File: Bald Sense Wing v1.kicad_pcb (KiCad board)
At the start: 4 copper layers, 50.8 x 22.9 mm, 43 parts, among them J1 feather long, J2 feather short, J3 1140084168, Q1 Q_PNP_BEC, Q2 Q_NPN_BEC, U1 APDS-9960, U2 DS3231MZ, U3 SHT30-DIS, U4 MIC5504-3.3YM5, U5 CMM-4737DT-26186-TR

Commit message: Finished v1 layout
Thanks to everyone on the stream!
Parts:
- moved JP6 18.3 mm to (61.6, 38.5)
- moved JP2 2.49 mm to (50.6, 35.6), turned to 90 degrees
- moved JP1 1.88 mm to (34.0, 43.9), turned to 0 degrees
- moved C1 1.80 mm to (69.9, 42.4)
- moved C4 0.84 mm to (69.1, 36.7), turned to 270 degrees
- moved U3 0.13 mm to (73.5, 36.7), turned to 180 degrees
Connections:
- J1 pad 11: /SD-CS -> /SD_CS
- J1 pad 12: /SD-CD -> /SD_CD
- J1 pad 8: /SHT30-ALERT -> /Batt_Meas
- J1 pad 9: /Batt_Meas -> /Batt_Meas_En
- J2 pad 3: /PDM_CLK -> /DS3231_RST
- J2 pad 4: /PDM_DATA -> /DS3231_INT
- J2 pad 5: /DS3231_RST -> /32KHz
- J2 pad 6: /DS3231_INT -> /PDM_CLK
- J2 pad 7: /32KHz -> /PDM_DATA
- J2 pad 8: /Batt_Meas_En -> /SHT30_ALERT
- JP3 pad 2: /SHT30-ALERT -> /SHT30_ALERT
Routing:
- net +BATT: track 0.00 -> 56.5 mm, vias 0 -> 2
- net +3V3: track 0.00 -> 45.4 mm, vias 0 -> 8
- net /VBAT: track 0.00 -> 38.1 mm, vias 0 -> 1
- net GND: track 0.00 -> 34.7 mm, vias 0 -> 19
- net /APDS_INT: track 0.00 -> 32.9 mm, vias 0 -> 4
- net /PDM_DATA: track 0.00 -> 32.7 mm
- net /PDM_CLK: track 0.00 -> 30.9 mm
- net /SD_DIn: track 0.00 -> 29.5 mm, vias 0 -> 1
- net /SD_CD: track 0.00 -> 28.5 mm
- net /VUSB_Meas: track 0.00 -> 28.4 mm
- net /SCL: track 2.77 -> 29.9 mm, vias 0 -> 2
- net /SD_DOut: track 0.00 -> 27.0 mm, vias 0 -> 2
- net /SD_CLK: track 0.00 -> 25.6 mm, vias 0 -> 1
- net /SDA: track 2.77 -> 27.9 mm, vias 0 -> 1
- net /SHT30_ALERT: track 0.00 -> 24.8 mm
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- added copper zone on In2.3v3.Cu, net +3V3
- added copper zone on B.Cu, net GND
- added copper zone on F.Cu, net GND
- added copper zone on In1.Gnd.Cu, net GND
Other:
- board text added: "Sound, Humidity, Incandescence, Temperature sensor"

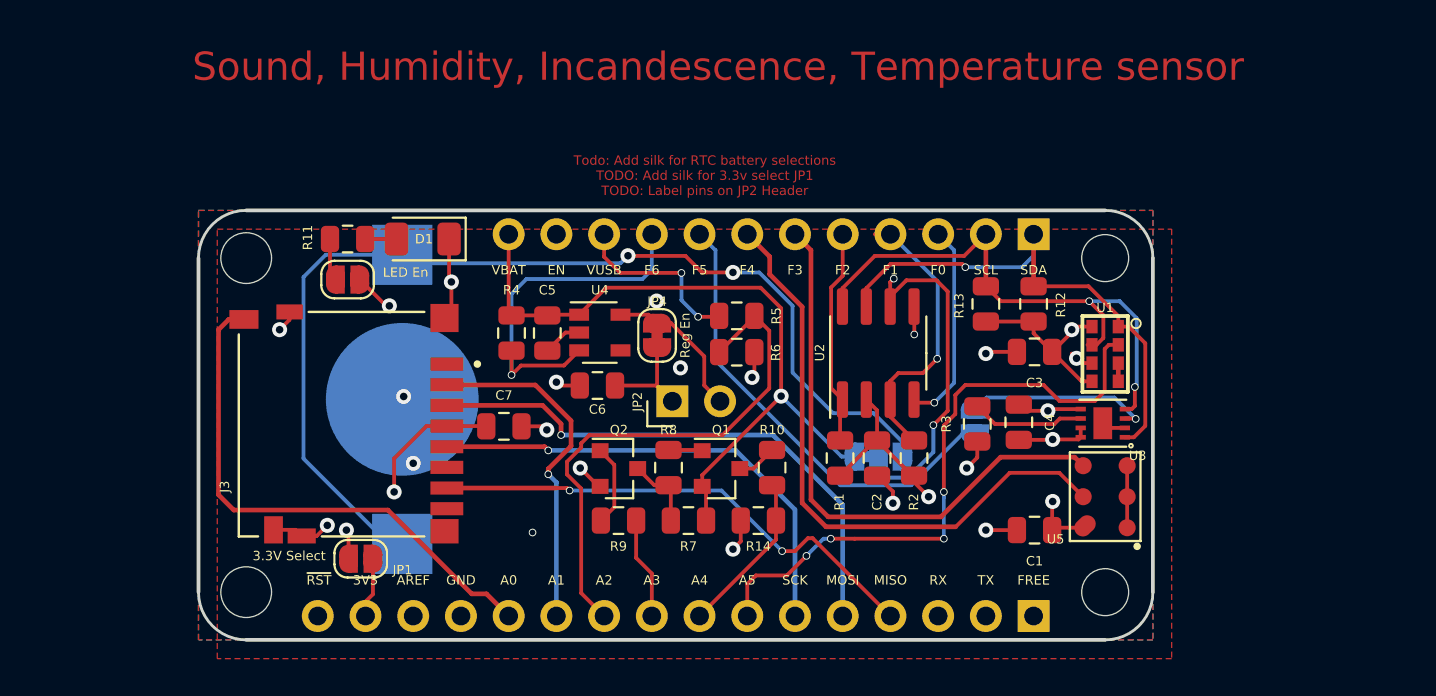
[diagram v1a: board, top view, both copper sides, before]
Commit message: Fixed courtyards and updated silkscreens
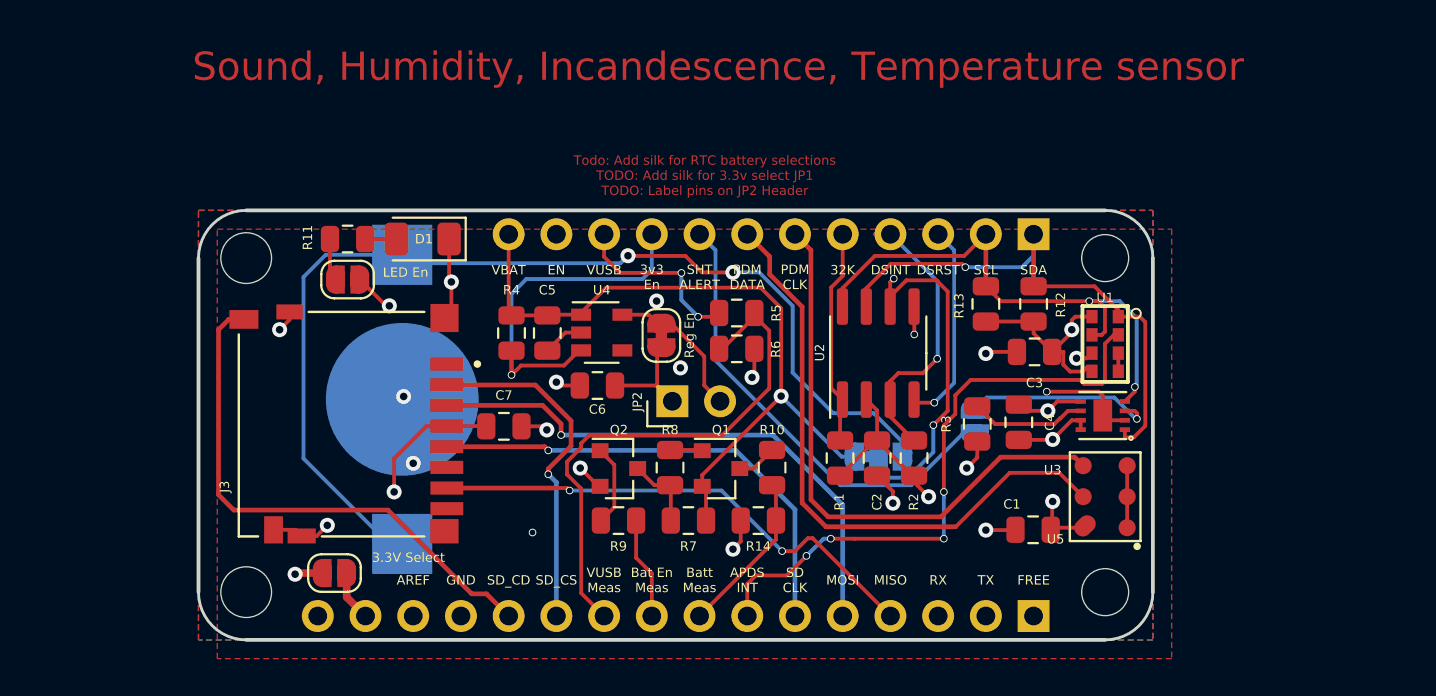
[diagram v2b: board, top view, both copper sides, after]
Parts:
- moved JP1 1.59 mm to (32.6, 44.7)
- moved U1 0.53 mm to (73.7, 32.5)
- moved U3 0.41 mm to (73.5, 36.3)
- moved JP4 0.23 mm to (50.0, 32.1)
- moved R6 0.18 mm to (54.1, 32.8)
- moved R5 0.15 mm to (54.1, 30.9)
- moved U4 0.10 mm to (46.9, 31.9)
- moved R8 0.08 mm to (50.5, 39.1)
- moved C1 0.08 mm to (69.8, 42.4)
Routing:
- net GND: track 34.7 -> 39.3 mm, vias 19 -> 20
- net +3V3: track 45.4 -> 46.7 mm
- net /SDA: track 27.9 -> 28.8 mm
- net /SCL: track 29.9 -> 29.0 mm
- net Net-(JP3-Pad1): track 9.88 -> 10.5 mm
- net /3v3_feather: track 3.21 -> 2.70 mm
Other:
- board text added: "32K"
- board text added: "3v3 En"
- board text added: "APDS INT"
- board text added: "Bat En Meas"
- board text added: "Batt Meas"
- board text added: "DSINT"
- board text added: "DSRST"
- board text added: "PDM CLK"
- board text added: "PDM DATA"
- board text added: "SD CLK"
- board text added: "SD_CD"
- board text added: "SD_CS"
- board text added: "SHT ALERT"
- board text added: "VUSB Meas"
- board text removed: "3V3"
- board text removed: "A0"
- board text removed: "A1"
- board text removed: "A2"
- board text removed: "A3"
- board text removed: "A4"
- board text removed: "A5"
- board text removed: "F0"
- board text removed: "F1"
- board text removed: "F2"
- board text removed: "F3"
- board text removed: "F4"
- board text removed: "F5"
- board text removed: "F6"
- board text removed: "SCK"
- board text removed: "~RST"

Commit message: Cleaned up silkscreens and submitted board
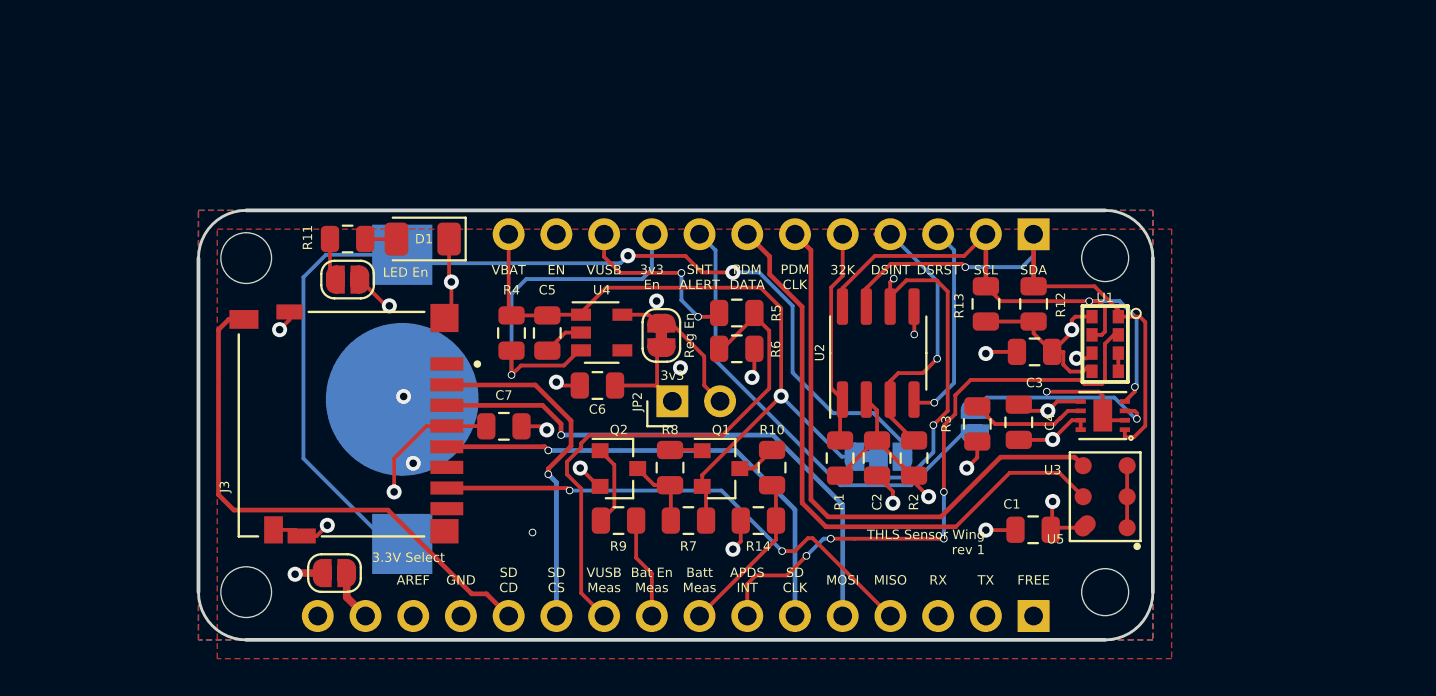
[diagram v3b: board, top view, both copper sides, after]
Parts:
- added REF**: OSHW-Logo_5.7x6mm_SilkScreen, Symbol:OSHW-Logo_5.7x6mm_SilkScreen, B.Cu at (72.9, 36.4)
- You can put a battery here!: renamed from BT1
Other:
- board text added: "3v3"
- board text added: "Coin"
- board text added: "LiPo"
- board text added: "SD CD"
- board text added: "SD CS"
- board text added: "THLS Sensor Wing james@baldengineer.com Rev1 Hi to everyone who helped on the Twitch Stream!"
- board text added: "THLS Sensor Wing rev 1"
- board text removed: "SD_CD"
- board text removed: "SD_CS"
- board text removed: "Sound, Humidity, Incandescence, Temperature sensor"
- board text removed: "Todo: Add silk for RTC battery selections TODO: Add silk for 3.3v select JP1 TODO: Label pins on JP2 Header"
